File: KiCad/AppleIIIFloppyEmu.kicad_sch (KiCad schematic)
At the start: 7 parts, among them J1 Apple III Int/Ext Floppy Port, J2 FloppyEmu / disk ][, J3 Unused

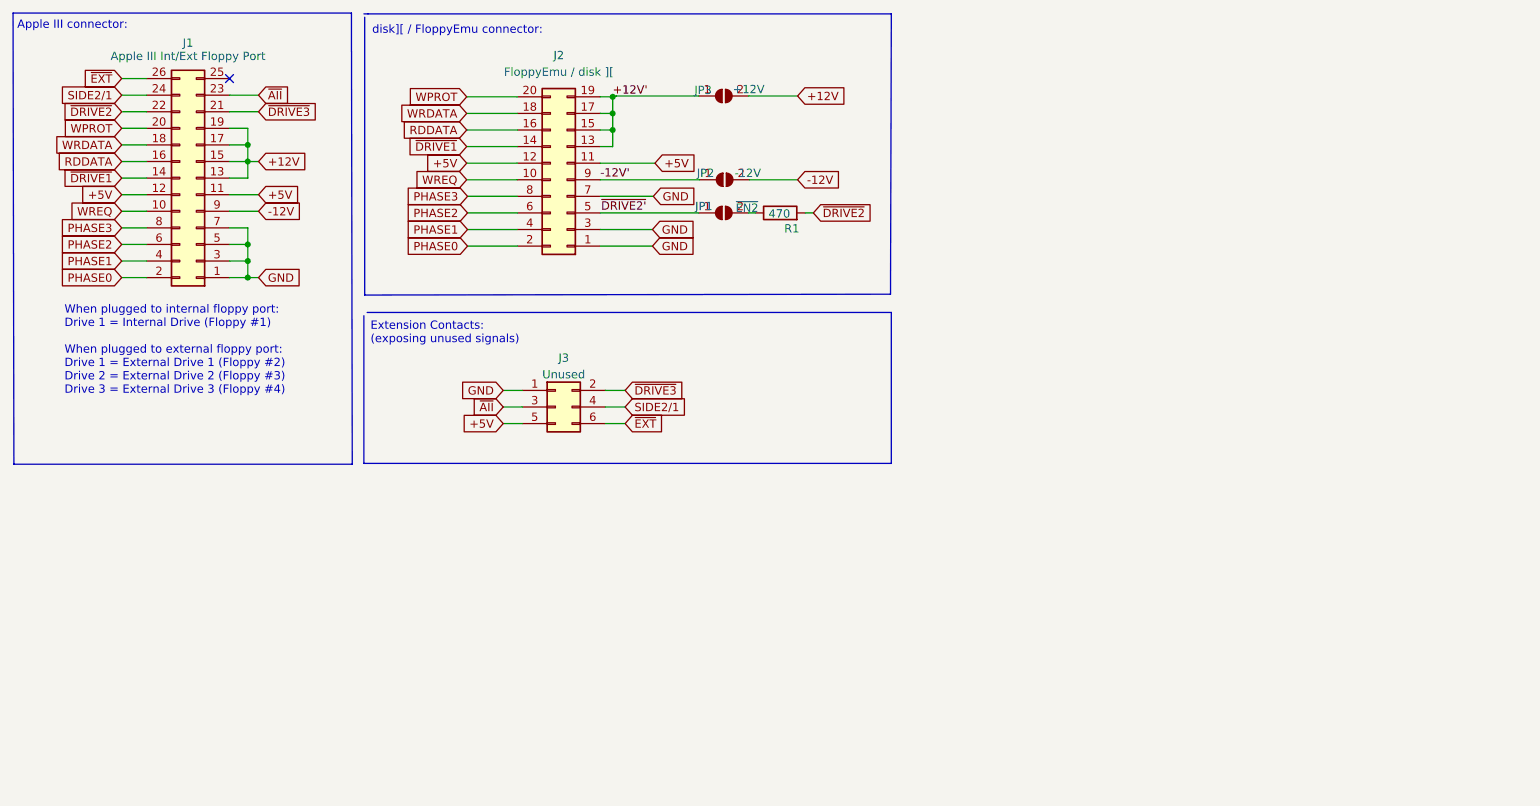
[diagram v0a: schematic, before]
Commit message: Updated README. Update to rev 1.1.
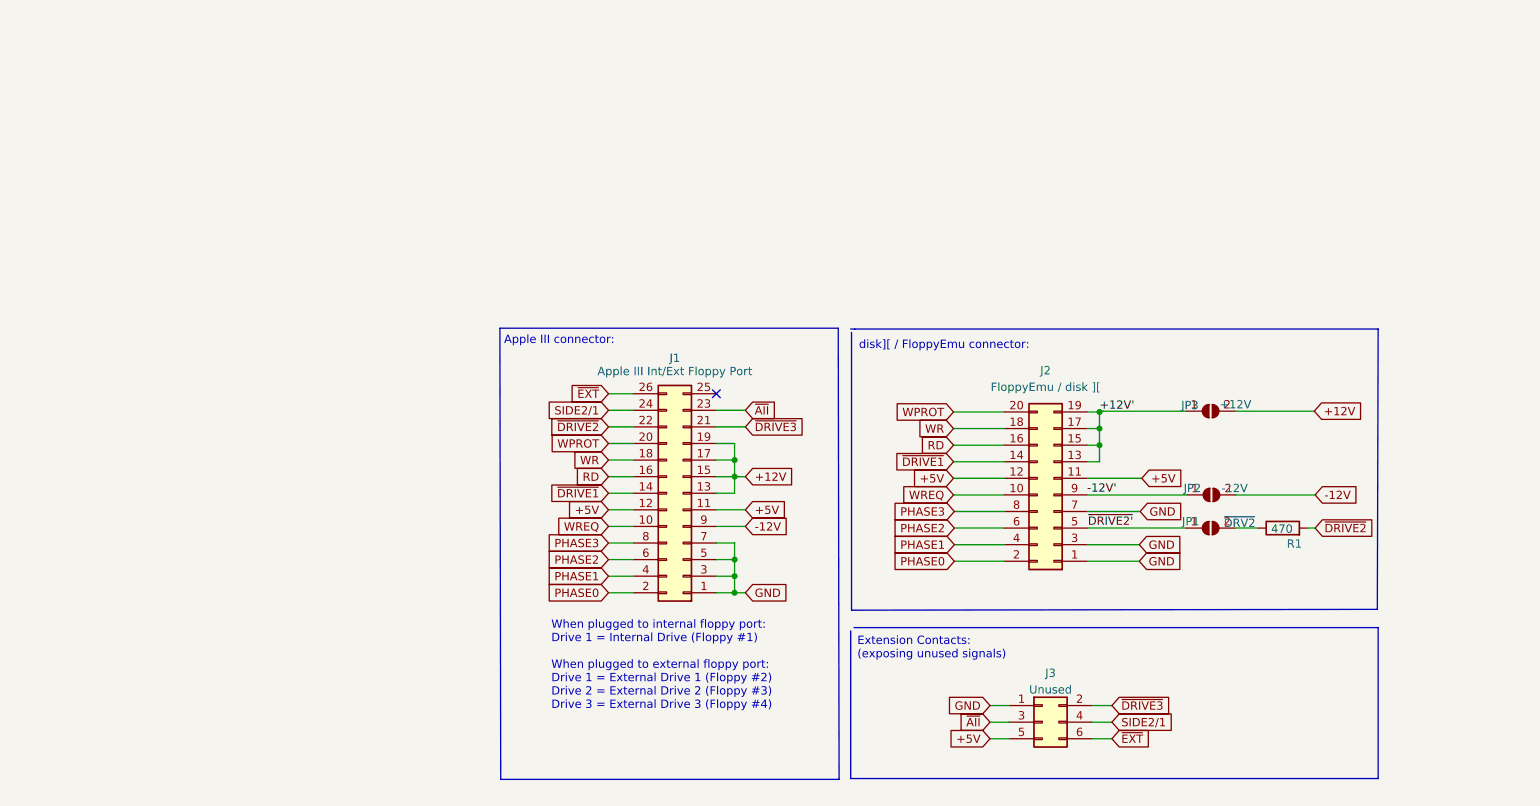
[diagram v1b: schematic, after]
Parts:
- JP1: value ~{EN2} -> ~{DRV2}
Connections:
- net RDDATA renamed RD
- net WRDATA renamed WR
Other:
- moved on the sheet: J1, J2, J3, JP1, JP2, JP3, R1

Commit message: Updated to v2.0: properly handle Apple /// Disk logic when SOS keeps the internal and one external drive spinning concurrently, while alternating the access to both drives. SOS uses this feature when copying volumes: it keeps the internal drive and one of the external drives both spinning, while copying data. This feature is not possible with Apple II drives. However, since Apple /// can enable two drives concurrently, it is necessary to also consider the "INT/EXT" signal. Added a simple OR-gate to combine the DRIVE+INT/EXT singals: both need to be LOW to enable the Apple II drive (or FloppyEmu).
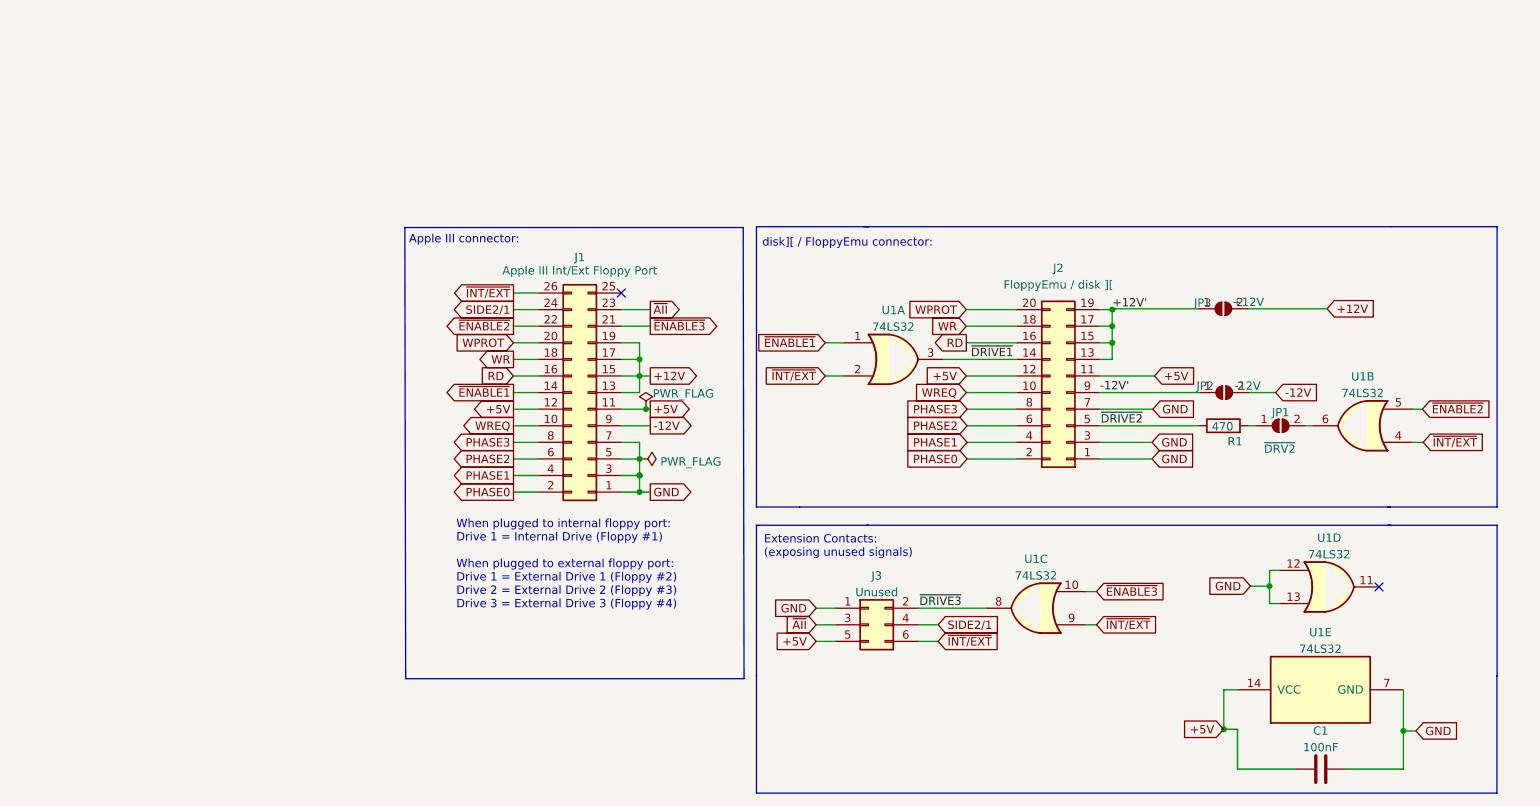
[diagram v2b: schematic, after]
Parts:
- added C1: 100nF, Capacitor_THT:C_Disc_D4.7mm_W2.5mm_P5.00mm, symbol Device:C
- added U1: 74LS32, Package_DIP:DIP-14_W7.62mm_Socket_LongPads, symbol 74xx:74LS32
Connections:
- net +5V: now also C1.1, U1.14 (VCC)
- net GND: now also C1.2, U1.12, U1.13, U1.7 (GND)
- net ~{DRIVE1}: now also U1.3; no longer J1.14 (Pin_14)
- net ~{DRIVE2}: now also J2.5 (Pin_5), R1.1; no longer J1.22 (Pin_22), R1.2
- net ~{DRIVE3}: now also U1.8; no longer J1.21 (Pin_21)
- net at JP1.2 (B): now also U1.6; no longer R1.1
- net ~{DRIVE2'}: no longer names the net of JP1.1 (A)
- net ~{DRIVE2'}: now also R1.2; no longer J2.5 (Pin_5)
- net ~{EXT} renamed ~{INT/EXT}
- net ~{INT/EXT}: now also U1.2, U1.4, U1.9
- new net ~{ENABLE1}: J1.14 (Pin_14), U1.1
- new net ~{ENABLE2}: J1.22 (Pin_22), U1.5
- new net ~{ENABLE3}: J1.21 (Pin_21), U1.10
- no-connect marks 1 -> 2
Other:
- moved on the sheet: J1, J2, J3, JP1, JP2, JP3, R1

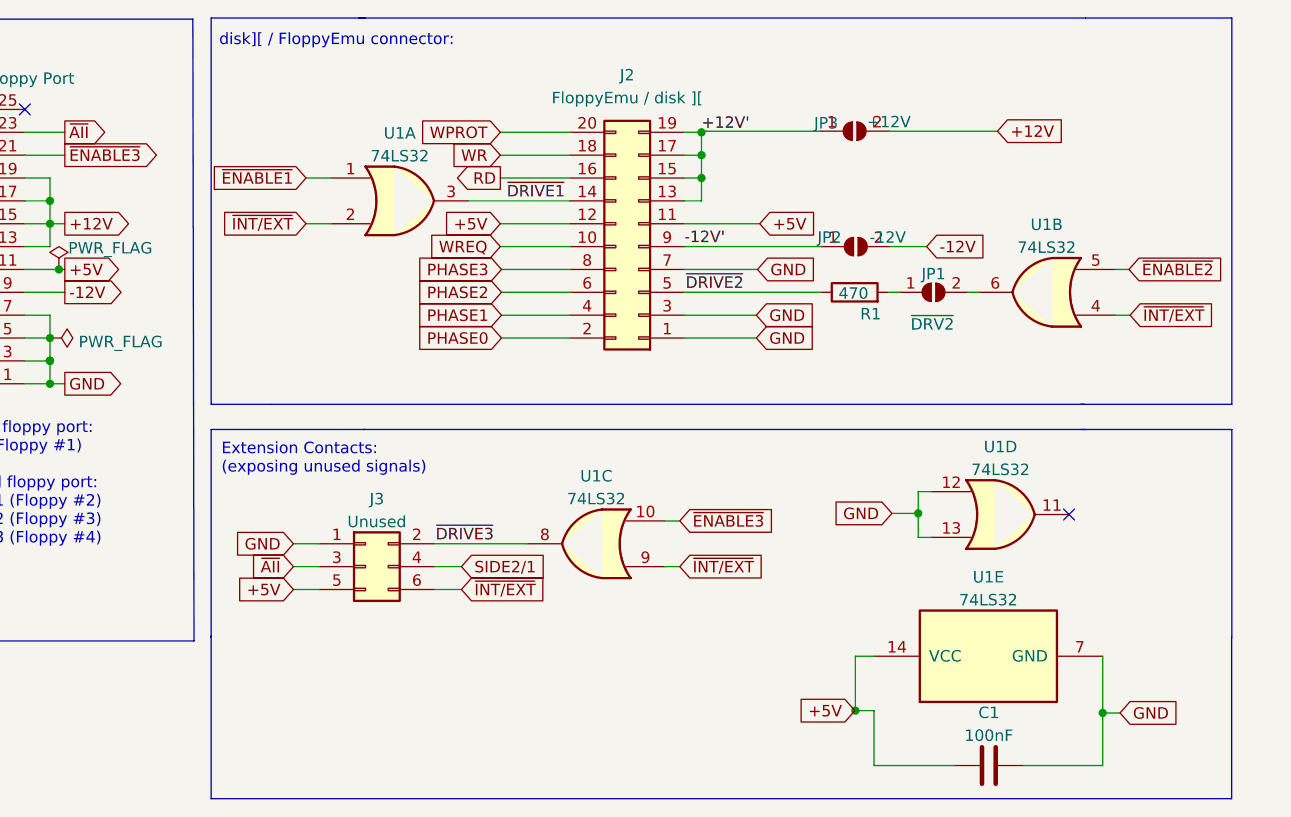
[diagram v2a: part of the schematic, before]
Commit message: Added optional pull-ups to ENBL1+2 to allow use of 74HCT32 ICs. The pull-ups (R2+R3) are not strictly required for 74LS32 ICs (but recommended anyway). R3 may be soldered on the top side, before soldering the IC socket. Alternatively R3 may be soldered to the bottom side of the PCB (also before soldering the IC socket).
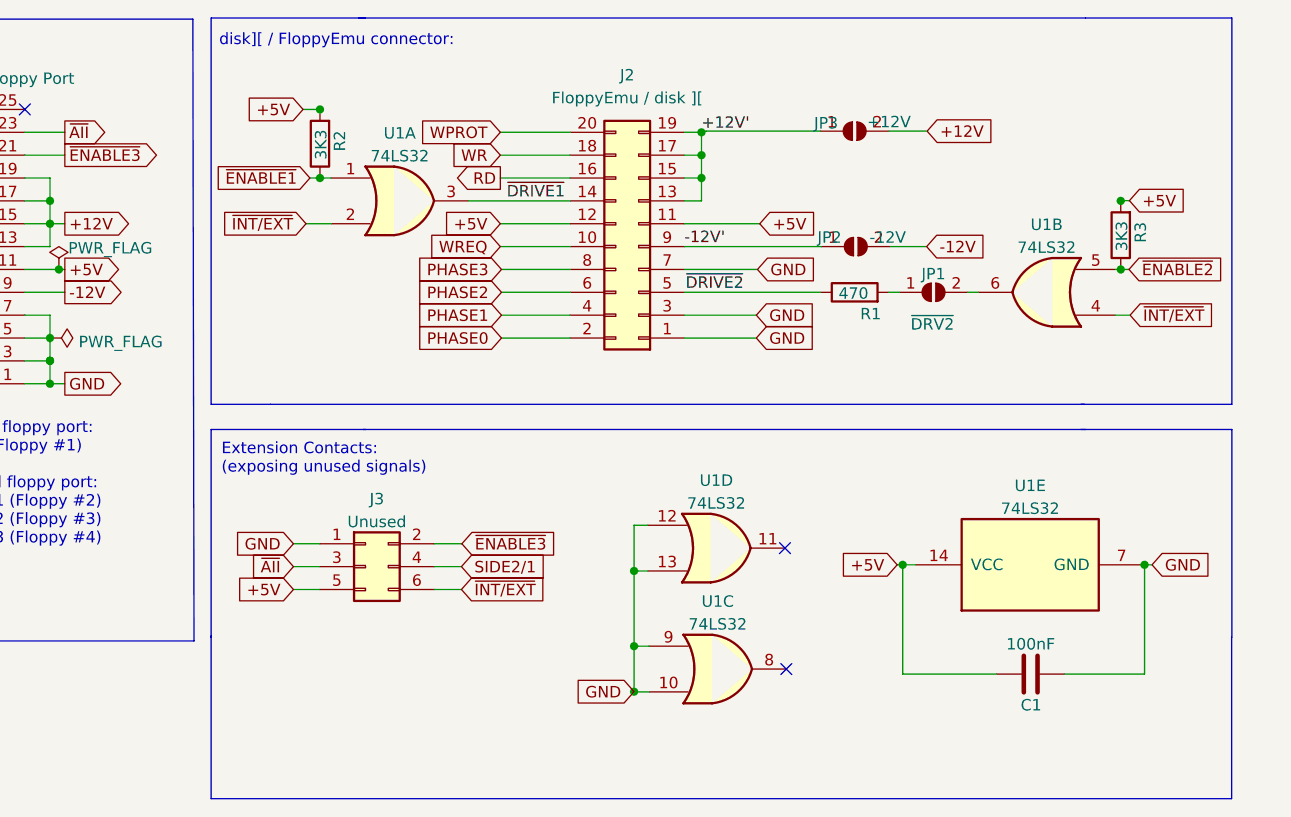
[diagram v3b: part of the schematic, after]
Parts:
- added R2, R3: 3K3, Resistor_THT:R_Axial_DIN0207_L6.3mm_D2.5mm_P10.16mm_Horizontal, symbol Device:R
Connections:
- net +5V: now also R2.2, R3.2
- net GND: now also U1.10, U1.9
- net ~{ENABLE1}: now also R2.1
- net ~{ENABLE2}: now also R3.1
- net ~{ENABLE3}: now also J3.2 (Pin_2); no longer U1.10
- net ~{INT/EXT}: no longer U1.9
- net ~{DRIVE3}: no longer names the net of U1.8
- net ~{DRIVE3}: no longer J3.2 (Pin_2)
- no-connect marks 2 -> 3
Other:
- moved on the sheet: C1, U1C, U1D, U1E
